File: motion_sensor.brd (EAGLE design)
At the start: 35 x 35 mm, 49 parts, among them J1 AVR_SPI_PRG_6PTH, J2 FTDI_DEVICERA_SMT, J3 3-PIN SMD, U1 LP2985A-33DBVTE4, U2 nRF8001, U4 ATMEGA328P_VQFNVQFN, Y1 16MHz, Y2 FC-255 32.7680K-A3, Y4 16MHz

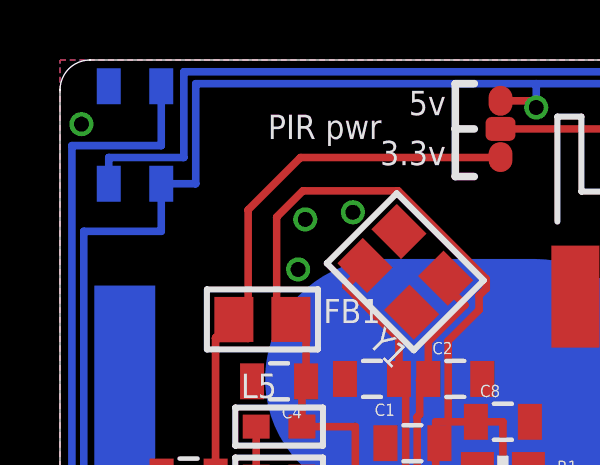
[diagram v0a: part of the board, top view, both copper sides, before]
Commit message: Add OSH logo. Add png versions of schematic and pcb.
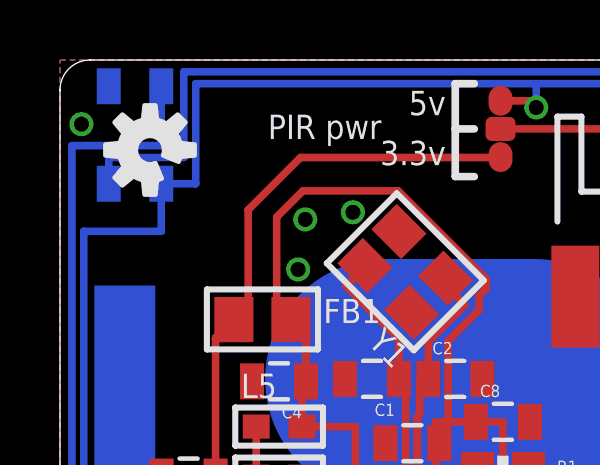
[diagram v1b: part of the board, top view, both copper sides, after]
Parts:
- added LOGO1: OSHW-LOGOS, SparkFun-Aesthetics:OSHW-LOGO-S
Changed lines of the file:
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@@
 </element>
 <element name="JMP1" library="jump-0r-smd" package="C0R-JMP" value="0R-JUMPC" x="14.684375" y="32.7025" smashed="yes"/>
+<element name="LOGO1" library="SparkFun-Aesthetics" package="OSHW-LOGO-S" value="OSHW-LOGOS" x="3" y="32" rot="R45"/>
 </elements>
 <signals>
